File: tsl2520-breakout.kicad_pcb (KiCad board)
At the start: 2 copper layers, 25 x 18.5 mm, 13 parts, among them J1 Conn_01x08, U1 TSL2585, U2 MIC5365-1.8YC5

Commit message: Rename project files and identifiers
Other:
- board text added: "TSL2520 TSL2521 TCS3410"
- board text removed: "TSL2520 TSL2521 TSL2585 TCS3410"
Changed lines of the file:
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@@
   (paper "USLetter")
   (title_block
-    (title "TSL2585 Sensor Breakout Board")
+    (title "TSL2520 Sensor Breakout Board")
     (date "2023-11-27")
     (rev "A")
@@
     (property "Manufacturer" "Vishay Dale")
     (property "Manufacturer PN" "CRCW060310K0JNEA")
-    (property "Sheetfile" "tsl2585-breakout.kicad_sch")
+    (property "Sheetfile" "tsl2520-breakout.kicad_sch")
     (property "Sheetname" "")
     (property "Supplier" "Digi-Key")
@@
     (property "Manufacturer" "Vishay Dale")
     (property "Manufacturer PN" "CRCW060310K0JNEA")
-    (property "Sheetfile" "tsl2585-breakout.kicad_sch")
+    (property "Sheetfile" "tsl2520-breakout.kicad_sch")
     (property "Sheetname" "")
     (property "Supplier" "Digi-Key")
@@
     (property "Manufacturer" "")
     (property "Manufacturer PN" "")
-    (property "Sheetfile" "tsl2585-breakout.kicad_sch")
+    (property "Sheetfile" "tsl2520-breakout.kicad_sch")
     (property "Sheetname" "")
     (property "Supplier" "")
@@
     (property "Manufacturer" "ams OSRAM")
     (property "Manufacturer PN" "TSL25853PM")
-    (property "Sheetfile" "tsl2585-breakout.kicad_sch")
+    (property "Sheetfile" "tsl2520-breakout.kicad_sch")
     (property "Sheetname" "")
     (property "Supplier" "Digi-Key")
@@
     (property "Manufacturer" "Microchip Technology")
     (property "Manufacturer PN" "MIC5365-1.8YC5-TR")
-    (property "Sheetfile" "tsl2585-breakout.kicad_sch")
+    (property "Sheetfile" "tsl2520-breakout.kicad_sch")
     (property "Sheetname" "")
     (property "Supplier" "Digi-Key")
@@
     (property "Manufacturer" "")
     (property "Manufacturer PN" "")
-    (property "Sheetfile" "tsl2585-breakout.kicad_sch")
+    (property "Sheetfile" "tsl2520-breakout.kicad_sch")
     (property "Sheetname" "")
     (property "Supplier" "")
@@
     (property "Manufacturer" "Samsung Electro-Mechanics")
     (property "Manufacturer PN" "CL05A475KQ5NRNC")
-    (property "Sheetfile" "tsl2585-breakout.kicad_sch")
+    (property "Sheetfile" "tsl2520-breakout.kicad_sch")
     (property "Sheetname" "")
     (property "Supplier" "Digi-Key")
@@
     (property "Manufacturer" "Samsung Electro-Mechanics")
     (property "Manufacturer PN" "CL10B105KA8NNNC")
-    (property "Sheetfile" "tsl2585-breakout.kicad_sch")
+    (property "Sheetfile" "tsl2520-breakout.kicad_sch")
     (property "Sheetname" "")
     (property "Supplier" "LCSC")
@@
     (property "Manufacturer" "Vishay Dale")
     (property "Manufacturer PN" "CRCW060310K0JNEA")
-    (property "Sheetfile" "tsl2585-breakout.kicad_sch")
+    (property "Sheetfile" "tsl2520-breakout.kicad_sch")
     (property "Sheetname" "")
     (property "Supplier" "Digi-Key")
@@
     (property "Manufacturer" "Samsung Electro-Mechanics")
     (property "Manufacturer PN" "CL05A105KQ5NNNC")
-    (property "Sheetfile" "tsl2585-breakout.kicad_sch")
+    (property "Sheetfile" "tsl2520-breakout.kicad_sch")
     (property "Sheetname" "")
     (property "Supplier" "LCSC")
@@
     (property "Manufacturer" "Samsung Electro-Mechanics")
     (property "Manufacturer PN" "CL10B105KA8NNNC")
-    (property "Sheetfile" "tsl2585-breakout.kicad_sch")
+    (property "Sheetfile" "tsl2520-breakout.kicad_sch")
     (property "Sheetname" "")
     (property "Supplier" "LCSC")
@@
     (property "Manufacturer" "Yaego")
     (property "Manufacturer PN" "AC0402JR-0722RL")
-    (property "Sheetfile" "tsl2585-breakout.kicad_sch")
+    (property "Sheetfile" "tsl2520-breakout.kicad_sch")
     (property "Sheetname" "")
     (property "Supplier" "LCSC")
@@
     (property "Manufacturer" "")
     (property "Manufacturer PN" "")
-    (property "Sheetfile" "tsl2585-breakout.kicad_sch")
+    (property "Sheetfile" "tsl2520-breakout.kicad_sch")
     (property "Sheetname" "")
     (property "Supplier" "")
@@
     )
   )
-  (gr_rect (start 53.5 32.3) (end 54.5 31.3)
+  (gr_rect (start 53.5 30.5) (end 54.5 31.5)
     (stroke (width 0.12) (type solid)) (fill solid) (layer "B.SilkS"))
-  (gr_rect (start 53.5 30.7) (end 54.5 29.7)
+  (gr_rect (start 53.5 33.7) (end 54.5 34.7)
     (stroke (width 0.12) (type solid)) (fill solid) (layer "B.SilkS"))
-  (gr_rect (start 53.5 35.5) (end 54.5 34.5)
-    (stroke (width 0.12) (type solid)) (fill solid) (layer "B.SilkS"))
-  (gr_rect (start 53.5 33.9) (end 54.5 32.9)
+  (gr_rect (start 53.5 32.1) (end 54.5 33.1)
     (stroke (width 0.12) (type solid)) (fill solid) (layer "B.SilkS"))
   (gr_line (start 42.5 23) (end 42.5 41)
@@
   (gr_line (start 55 26) (end 55 38.37868)
     (stroke (width 0.05) (type default)) (layer "Edge.Cuts"))
-  (gr_text "TSL2520\nTSL2521\nTSL2585\nTCS3410" (at 53.2 35.7) (layer "B.SilkS")
+  (gr_text "TSL2520\nTSL2521\nTCS3410" (at 53.2 34.9) (layer "B.SilkS")
     (effects (font (size 1 1) (thickness 0.15)) (justify left bottom mirror))
   )
@@
     (members
       32a64b0f-d6b0-4789-9c33-70a0a10073d8
-      5463b71c-086f-4dd3-b3d0-8d389406444f
       6b5ae48a-f7e6-4fdb-95c4-cca5dc8ec693
       9db497a7-e0ff-44ae-b4d9-30eeedc5e270

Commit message: Update symbol, schematic, and PCB layout
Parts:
- U1: value TSL2585 -> TSL2520
- moved C1 0.55 mm to (40.8, 28.5)
- moved C2 0.55 mm to (40.2, 30.0)
- moved R1 0.55 mm to (39.7, 28.5)
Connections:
- U1 pad 1: Net-(U1-VDD) -> /SENSOR_INT
- U1 pad 2: /SENSOR_VSYNC -> Net-(U1-VDD)
- U1 pad 5: /SENSOR_INT -> /SENSOR_SDA
- U1 pad 6: /SENSOR_SDA -> /SENSOR_VSYNC
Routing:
- net /SENSOR_VSYNC: track 20.3 -> 16.2 mm, vias 2 -> 0
- net /SENSOR_INT: track 15.6 -> 18.7 mm
- net /SENSOR_SDA: track 14.4 -> 13.5 mm

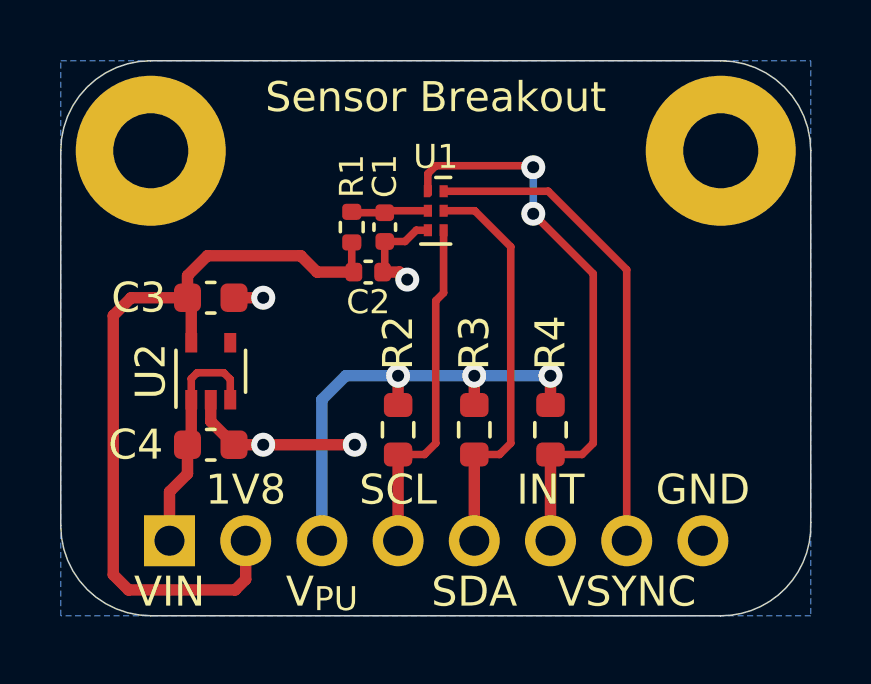
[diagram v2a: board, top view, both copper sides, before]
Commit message: Update breakout board design
Changes for KiCad v9 update and various silkscreen changes
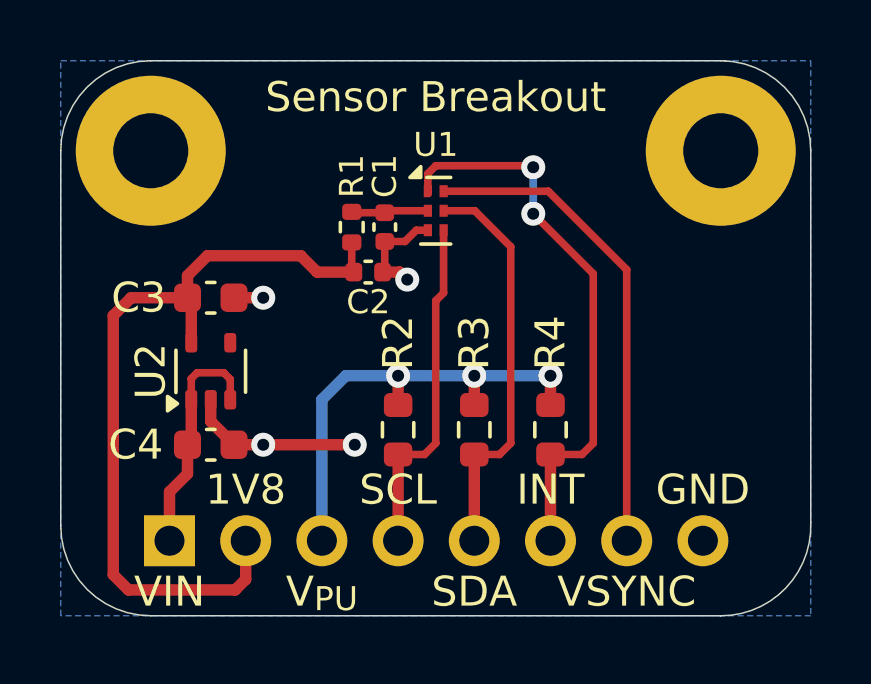
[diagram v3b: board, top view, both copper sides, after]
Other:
- board text added: "TCS3410"
- board text added: "TSL2520"
- board text added: "TSL2521"
- board text added: "TSL2522"
- board text removed: "TSL2520 TSL2521 TCS3410"
